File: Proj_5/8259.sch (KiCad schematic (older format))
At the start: 1 part

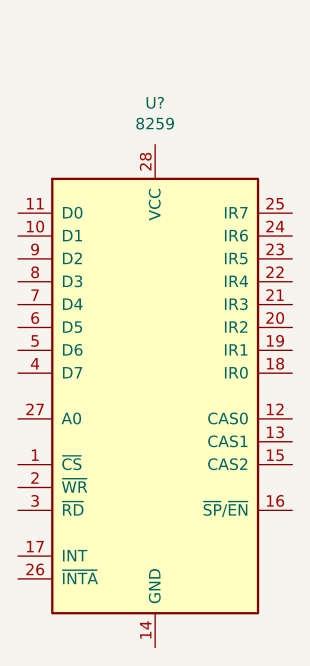
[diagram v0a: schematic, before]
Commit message: Added address decoding
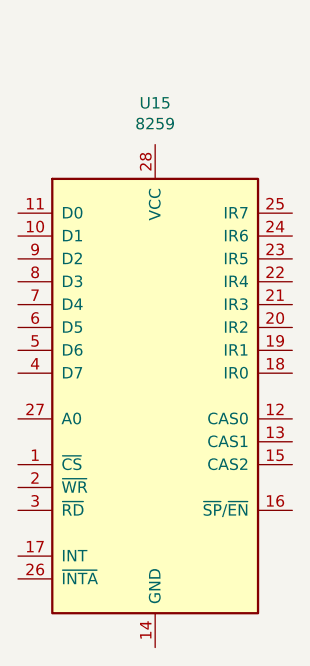
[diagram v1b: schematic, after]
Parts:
- gave numbers to parts that had none: 1
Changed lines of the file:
@@
 $EndDescr
 $Comp
-L Interface:8259 U?
+L Interface:8259 U15
 U 1 1 5EA9E11F
 P 5950 3750
-F 0 "U?" H 5950 5031 50  0000 C CNN
+F 0 "U15" H 5950 5031 50  0000 C CNN
 F 1 "8259" H 5950 4940 50  0000 C CNN
 F 2 "Package_DIP:DIP-28_W15.24mm" H 5950 3750 50  0001 C CIN

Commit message: Added Caps to Each Vcc per desc.
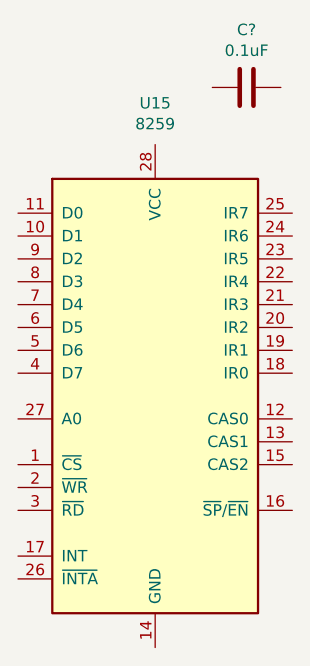
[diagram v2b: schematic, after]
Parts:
- added C?: 0.1uF, symbol Device:C
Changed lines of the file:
@@
 $Descr A4 11693 8268
 encoding utf-8
-Sheet 7 11
+Sheet 6 11
 Title ""
 Date ""
@@
 	1    0    0    -1
 $EndComp
+$Comp
+L Device:C C?
+U 1 1 5EA64E89
+P 6350 2400
+AR Path="/5EA98353/5EA64E89" Ref="C?"  Part="1"
+AR Path="/5EA99014/5EA64E89" Ref="C?"  Part="1"
+F 0 "C?" V 6098 2400 50  0000 C CNN
+F 1 "0.1uF" V 6189 2400 50  0000 C CNN
+F 2 "" H 6388 2250 50  0001 C CNN
+F 3 "~" H 6350 2400 50  0001 C CNN
+	1    6350 2400
+	0    1    1    0
+$EndComp
 $EndSCHEMATC
